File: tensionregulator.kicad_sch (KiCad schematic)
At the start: 5 parts, among them U3 ISU0224S05, U4 TCR5AM055

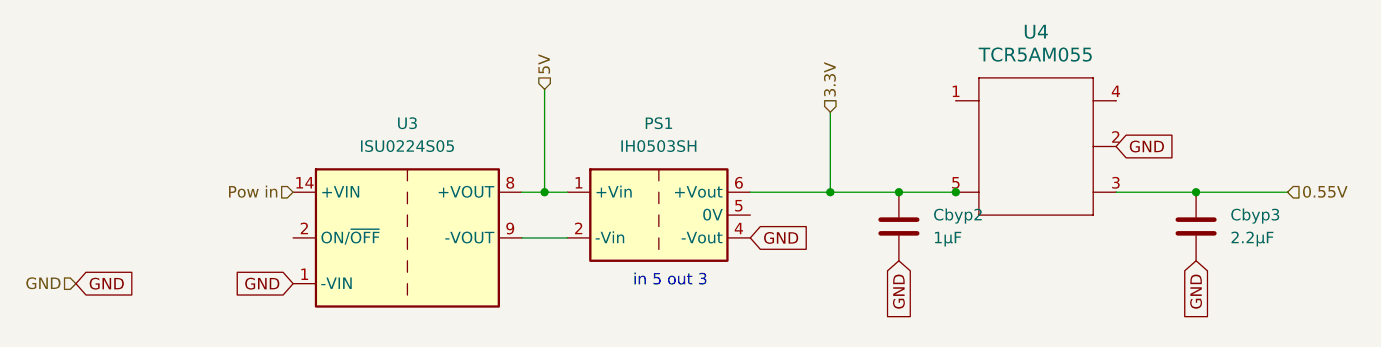
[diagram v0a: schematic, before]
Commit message: changed relays
opted for latching dual coil relays,  fixed broken symbols and added a hierarchical sheet
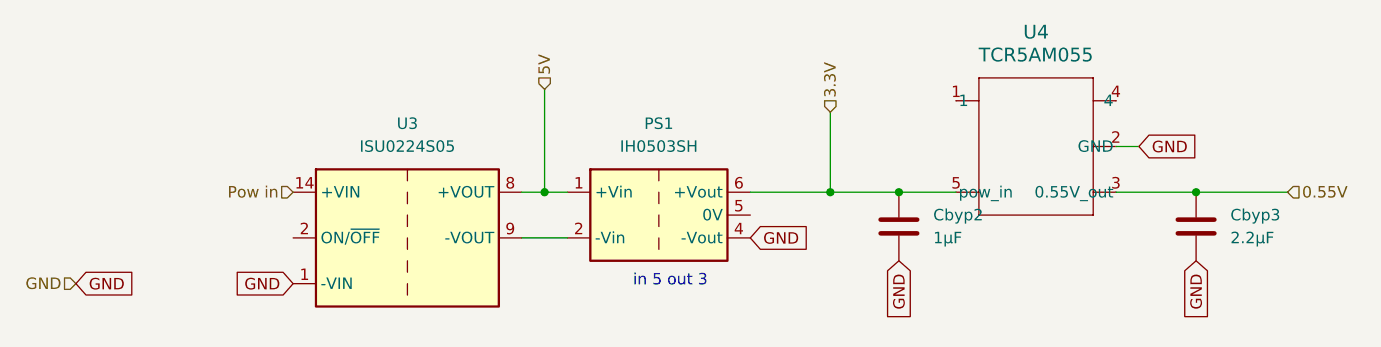
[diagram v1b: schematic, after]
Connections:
- net 0.55V: now also U4.3 (0.55V_out)
- net GND: now also U4.2 (GND)
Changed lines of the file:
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@@
-	)
-	(junction
-		(at 176.5046 80.01)
-		(diameter 0)
-		(color 0 0 0 0)
 	)
 	(junction
@@
 	(wire
 		(pts
-			(xy 170.18 80.01) (xy 176.5046 80.01)
+			(xy 170.18 80.01) (xy 176.53 80.01)
 		)
 		(stroke
@@
 	(wire
 		(pts
-			(xy 176.5046 80.01) (xy 176.53 80.01)
-		)
-		(stroke
-			(width 0)
-			(type default)
-		)
-	)
-	(wire
-		(pts
 			(xy 130.81 68.58) (xy 130.81 80.01)
 		)
@@
 		(pts
 			(xy 130.81 80.01) (xy 133.35 80.01)
+		)
+		(stroke
+			(width 0)
+			(type default)
+		)
+	)
+	(wire
+		(pts
+			(xy 194.31 74.93) (xy 196.85 74.93)
 		)
 		(stroke
@@
 	(global_label "GND"
 		(shape input)
-		(at 194.31 74.93 0)
+		(at 196.85 74.93 0)
 		(fields_autoplaced yes)
 		(effects
@@
 		)
 		(property "Intersheetrefs" "${INTERSHEET_REFS}"
-			(at 200.5115 74.93 0)
+			(at 203.0515 74.93 0)
 			(effects
 				(font
@@
 			)
 			(justify left)
+		)
+	)
+	(symbol
+		(lib_id "Device:C")
+		(at 203.2 83.82 0)
+		(unit 1)
+		(exclude_from_sim no)
+		(in_bom yes)
+		(on_board yes)
+		(dnp no)
+		(fields_autoplaced yes)
+		(property "Reference" "Cbyp3"
+			(at 207.01 82.5499 0)
+			(effects
+				(font
+					(size 1.27 1.27)
+				)
+				(justify left)
+			)
+		)
+		(property "Value" "2.2μF"
+			(at 207.01 85.0899 0)
+			(effects
+				(font
+					(size 1.27 1.27)
+				)
+				(justify left)
+			)
+		)
+		(property "Footprint" "Capacitor_THT:CP_Axial_L10.0mm_D4.5mm_P15.00mm_Horizontal"
+			(at 204.1652 87.63 0)
+			(effects
+				(font
+					(size 1.27 1.27)
+				)
+				(hide yes)
+			)
+		)
+		(property "Datasheet" "~"
+			(at 203.2 83.82 0)
+			(effects
+				(font
+					(size 1.27 1.27)
+				)
+				(hide yes)
+			)
+		)
+		(property "Description" "Unpolarized capacitor"
+			(at 203.2 83.82 0)
+			(effects
+				(font
+					(size 1.27 1.27)
+				)
+				(hide yes)
+			)
+		)
+		(pin "2"
+		)
+		(pin "1"
+		)
+		(instances
+			(project "recruitment"
+				(path "/bdc7face-9f7c-4701-80bb-4cc144448db1/209c530a-7e9c-4ebf-a627-f537295344ec"
+					(reference "Cbyp3")
+					(unit 1)
+				)
+			)
+		)
+	)
+	(symbol
+		(lib_id "Converter_DCDC:IH0503SH")
+		(at 143.51 82.55 0)
+		(unit 1)
+		(exclude_from_sim no)
+		(in_bom yes)
+		(on_board yes)
+		(dnp no)
+		(fields_autoplaced yes)
+		(property "Reference" "PS1"
+			(at 143.51 72.39 0)
+			(effects
+				(font
+					(size 1.27 1.27)
+				)
+			)
+		)
+		(property "Value" "IH0503SH"
+			(at 143.51 74.93 0)
+			(effects
+				(font
+					(size 1.27 1.27)
+				)
+			)
+		)
+		(property "Footprint" "Converter_DCDC:Converter_DCDC_XP_POWER-IHxxxxSH_THT"
+			(at 116.84 88.9 0)
+			(effects
+				(font
+					(size 1.27 1.27)
+				)
+				(justify left)
+				(hide yes)
+			)
+		)
+		(property "Datasheet" "https://www.xppower.com/pdfs/SF_IH.pdf"
+			(at 170.18 90.17 0)
+			(effects
+				(font
+					(size 1.27 1.27)
+				)
+				(justify left)
+				(hide yes)
+			)
+		)
+		(property "Description" "XP Power 2W, 3000-6000 VDC Isolated DC/DC Converter Module, Dual Output Voltage ±3.3V, ±200mA, 5V Input Voltage, SIP"
+			(at 143.51 82.55 0)
+			(effects
+				(font
+					(size 1.27 1.27)
+				)
+				(hide yes)
+			)
+		)
+		(pin "4"
+		)
+		(pin "5"
+		)
+		(pin "2"
+		)
+		(pin "1"
+		)
+		(pin "6"
+		)
+		(instances
+			(project "recruitment"
+				(path "/bdc7face-9f7c-4701-80bb-4cc144448db1/209c530a-7e9c-4ebf-a627-f537295344ec"
+					(reference "PS1")
+					(unit 1)
+				)
+			)
 		)
 	)
@@
 			)
 		)
+		(pin "3"
+		)
 		(pin "1"
 		)
 		(pin "4"
 		)
+		(pin "2"
+		)
 		(pin "5"
-		)
-		(pin "3"
-		)
-		(pin "2"
 		)
 		(instances
@@
 					(unit 1)
 				)
-			)
-		)
-	)
-	(symbol
-		(lib_id "Device:C")
-		(at 203.2 83.82 0)
-		(unit 1)
-		(exclude_from_sim no)
-		(in_bom yes)
-		(on_board yes)
-		(dnp no)
-		(fields_autoplaced yes)
-		(property "Reference" "Cbyp3"
-			(at 207.01 82.5499 0)
-			(effects
-				(font
-					(size 1.27 1.27)
-				)
-				(justify left)
-			)
-		)
-		(property "Value" "2.2μF"
-			(at 207.01 85.0899 0)
-			(effects
-				(font
-					(size 1.27 1.27)
-				)
-				(justify left)
-			)
-		)
-		(property "Footprint" "Capacitor_THT:CP_Axial_L10.0mm_D4.5mm_P15.00mm_Horizontal"
-			(at 204.1652 87.63 0)
-			(effects
-				(font
-					(size 1.27 1.27)
-				)
-				(hide yes)
-			)
-		)
-		(property "Datasheet" "~"
-			(at 203.2 83.82 0)
-			(effects
-				(font
-					(size 1.27 1.27)
-				)
-				(hide yes)
-			)
-		)
-		(property "Description" "Unpolarized capacitor"
-			(at 203.2 83.82 0)
-			(effects
-				(font
-					(size 1.27 1.27)
-				)
-				(hide yes)
-			)
-		)
-		(pin "2"
-		)
-		(pin "1"
-		)
-		(instances
-			(project "recruitment"
-				(path "/bdc7face-9f7c-4701-80bb-4cc144448db1/209c530a-7e9c-4ebf-a627-f537295344ec"
-					(reference "Cbyp3")
-					(unit 1)
-				)
-			)
-		)
-	)
-	(symbol
-		(lib_id "Converter_DCDC:IH0503SH")
-		(at 143.51 82.55 0)
-		(unit 1)
-		(exclude_from_sim no)
-		(in_bom yes)
-		(on_board yes)
-		(dnp no)
-		(fields_autoplaced yes)
-		(property "Reference" "PS1"
-			(at 143.51 72.39 0)
-			(effects
-				(font
-					(size 1.27 1.27)
-				)
-			)
-		)
-		(property "Value" "IH0503SH"
-			(at 143.51 74.93 0)
-			(effects
-				(font
-					(size 1.27 1.27)
-				)
-			)
-		)
-		(property "Footprint" "Converter_DCDC:Converter_DCDC_XP_POWER-IHxxxxSH_THT"
-			(at 116.84 88.9 0)
-			(effects
-				(font
-					(size 1.27 1.27)
-				)
-				(justify left)
-				(hide yes)
-			)
-		)
-		(property "Datasheet" "https://www.xppower.com/pdfs/SF_IH.pdf"
-			(at 170.18 90.17 0)
-			(effects
-				(font
-					(size 1.27 1.27)
-				)
-				(justify left)
-				(hide yes)
-			)
-		)
-		(property "Description" "XP Power 2W, 3000-6000 VDC Isolated DC/DC Converter Module, Dual Output Voltage ±3.3V, ±200mA, 5V Input Voltage, SIP"
-			(at 143.51 82.55 0)
-			(effects
-				(font
-					(size 1.27 1.27)
-				)
-				(hide yes)
-			)
-		)
-		(pin "4"
-		)
-		(pin "5"
-		)
-		(pin "2"
-		)
-		(pin "1"
-		)
-		(pin "6"
-		)
-		(instances
-			(project "recruitment"
-				(path "/bdc7face-9f7c-4701-80bb-4cc144448db1/209c530a-7e9c-4ebf-a627-f537295344ec"
-					(reference "PS1")
-					(unit 1)
-				)
